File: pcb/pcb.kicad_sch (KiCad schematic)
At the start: 44 parts, among them J1 GPS Module Breakout, J2 MicroSD Card Breakout, U1 XIAO-ESP32-C5-DIP, U10 XIAO-ESP32-C5-DIP, U11 XIAO-ESP32-C5-DIP, U12 XIAO-ESP32-C5-DIP, U13 XIAO-ESP32-C5-DIP, U14 XIAO-ESP32-C5-DIP, U15 XIAO-ESP32-C5-DIP, U16 XIAO-ESP32-C5-DIP, U17 ESP32-S3 DevKitC-1, U18 LD1117V33, U19 SN74HC125N, U2 XIAO-ESP32-C5-DIP, U20 SN74HC138N, U21 SN74HC138N, U3 XIAO-ESP32-C5-DIP, U4 XIAO-ESP32-C5-DIP, U5 XIAO-ESP32-C5-DIP, U6 XIAO-ESP32-C5-DIP, U7 XIAO-ESP32-C5-DIP, U8 XIAO-ESP32-C5-DIP, U9 XIAO-ESP32-C5-DIP

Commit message: implement more feedback from red :D
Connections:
- net +5V: no longer U20.16 (VCC), U20.6 (G1), U21.16 (VCC)
- net CS 00: now also J2.1 (Pin_1); no longer C2.1, J2.6 (Pin_6), R1.1, U19.12 (4A)
- net GND: now also C2.2, U19.12 (4A)
- net +3.3V: now reaches C3.2, U18.2 (VO), U19.14 (VCC)
- net +3.3V: now also C2.1, J2.6 (Pin_6), R1.1, U20.16 (VCC), U20.6 (G1), U21.16 (VCC); no longer C2.2
- net at U19.11 (4Y): no longer J2.1 (Pin_1)
- no-connect marks 143 -> 144
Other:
- moved on the sheet: C2

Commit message: Add brownout protection
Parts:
- added C4: 47uF, Capacitor_THT:C_Disc_D5.0mm_W2.5mm_P2.50mm, symbol Device:C
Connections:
- net +5V: now also C4.2
- net GND: now also C4.1
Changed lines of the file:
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@@
 	)
 	(junction
+		(at 196.85 34.29)
+		(diameter 0)
+		(color 0 0 0 0)
+	)
+	(junction
 		(at 226.06 129.54)
 		(diameter 0)
@@
 	)
 	(junction
+		(at 196.85 24.13)
+		(diameter 0)
+		(color 0 0 0 0)
+	)
+	(junction
 		(at 87.63 212.09)
 		(diameter 0)
@@
 	(wire
 		(pts
+			(xy 204.47 25.4) (xy 196.85 25.4)
+		)
+		(stroke
+			(width 0)
+			(type default)
+		)
+	)
+	(wire
+		(pts
 			(xy 87.63 22.86) (xy 73.66 22.86)
 		)
@@
 	(wire
 		(pts
+			(xy 196.85 33.02) (xy 196.85 34.29)
+		)
+		(stroke
+			(width 0)
+			(type default)
+		)
+	)
+	(wire
+		(pts
 			(xy 226.06 191.77) (xy 226.06 207.01)
 		)
@@
 	(wire
 		(pts
+			(xy 196.85 25.4) (xy 196.85 24.13)
+		)
+		(stroke
+			(width 0)
+			(type default)
+		)
+	)
+	(wire
+		(pts
 			(xy 280.67 240.03) (xy 278.13 240.03)
 		)
@@
 	(wire
 		(pts
+			(xy 204.47 33.02) (xy 196.85 33.02)
+		)
+		(stroke
+			(width 0)
+			(type default)
+		)
+	)
+	(wire
+		(pts
 			(xy 133.35 143.51) (xy 133.35 147.32)
 		)
@@
 					(unit 1)
 				)
+			)
+		)
+	)
+	(symbol
+		(lib_id "Device:C")
+		(at 204.47 29.21 180)
+		(unit 1)
+		(body_style 1)
+		(exclude_from_sim no)
+		(in_bom yes)
+		(on_board yes)
+		(in_pos_files yes)
+		(dnp no)
+		(fields_autoplaced yes)
+		(property "Reference" "C4"
+			(at 208.28 27.9399 0)
+			(show_name no)
+			(do_not_autoplace no)
+			(effects
+				(font
+					(size 1.27 1.27)
+				)
+				(justify right)
+			)
+		)
+		(property "Value" "47uF"
+			(at 208.28 30.4799 0)
+			(show_name no)
+			(do_not_autoplace no)
+			(effects
+				(font
+					(size 1.27 1.27)
+				)
+				(justify right)
+			)
+		)
+		(property "Footprint" "Capacitor_THT:C_Disc_D5.0mm_W2.5mm_P2.50mm"
+			(at 203.5048 25.4 0)
+			(hide yes)
+			(show_name no)
+			(do_not_autoplace no)
+			(effects
+				(font
+					(size 1.27 1.27)
+				)
+			)
+		)
+		(property "Datasheet" ""
+			(at 204.47 29.21 0)
+			(hide yes)
+			(show_name no)
+			(do_not_autoplace no)
+			(effects
+				(font
+					(size 1.27 1.27)
+				)
+			)
+		)
+		(property "Description" "Unpolarized capacitor"
+			(at 204.47 29.21 0)
+			(hide yes)
+			(show_name no)
+			(do_not_autoplace no)
+			(effects
+				(font
+					(size 1.27 1.27)
+				)
+			)
+		)
+		(pin "1"
+		)
+		(pin "2"
+		)
+		(instances
+			(project "pcb"
+				(path "/177b52ef-cce2-4dab-a936-75649664352c"
+					(reference "C4")
+					(unit 1)
+				)

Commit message: Thicker tracks, remove redundant ground lines, mounting holes
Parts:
- added H1, H2, H3, H4: MountingHole, MountingHole:MountingHole_3.2mm_M3, symbol Mechanical:MountingHole

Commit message: Fix 15/16 ordering
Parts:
- renumbered R2 to R1, R11 to R10, R12 to R11, R13 to R12, R14 to R13, R15 to R14, R16 to R15, R17 to R16, R1 to R17, R3 to R2, R4 to R3, R5 to R4, R6 to R5, R7 to R6, R8 to R7, R9 to R8, R10 to R9, U16 to U15, U15 to U16
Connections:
- net CS 15: now also R15.2, U15.3 (GPIO25_D2); no longer R16.2, U16.3 (GPIO25_D2)
- net CS 16: now also R16.2, U16.3 (GPIO25_D2); no longer R15.2, U15.3 (GPIO25_D2)
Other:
- moved on the sheet: R15, R16, U15, U16

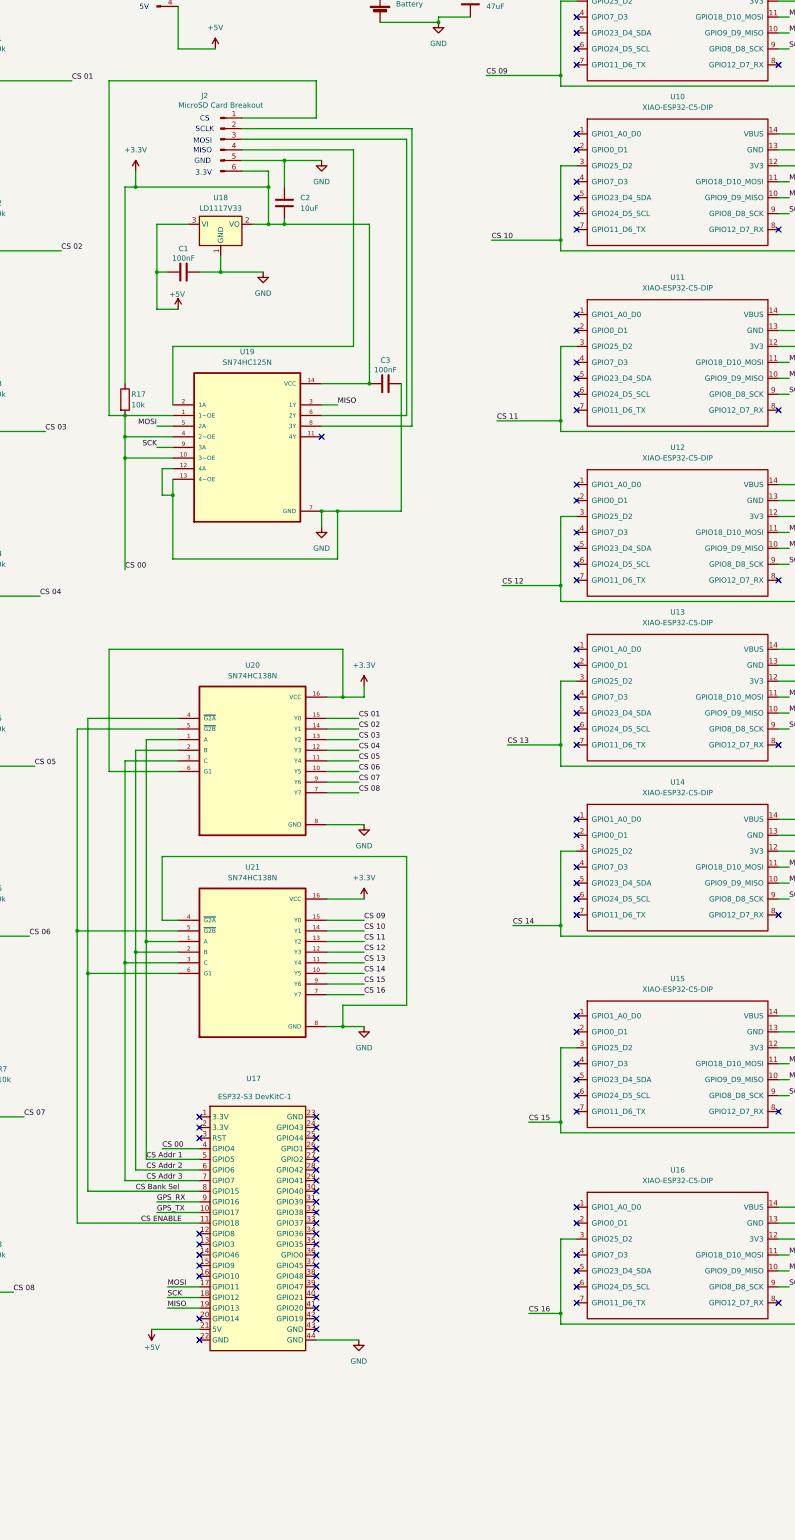
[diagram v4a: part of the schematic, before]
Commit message: add exhaust fan power
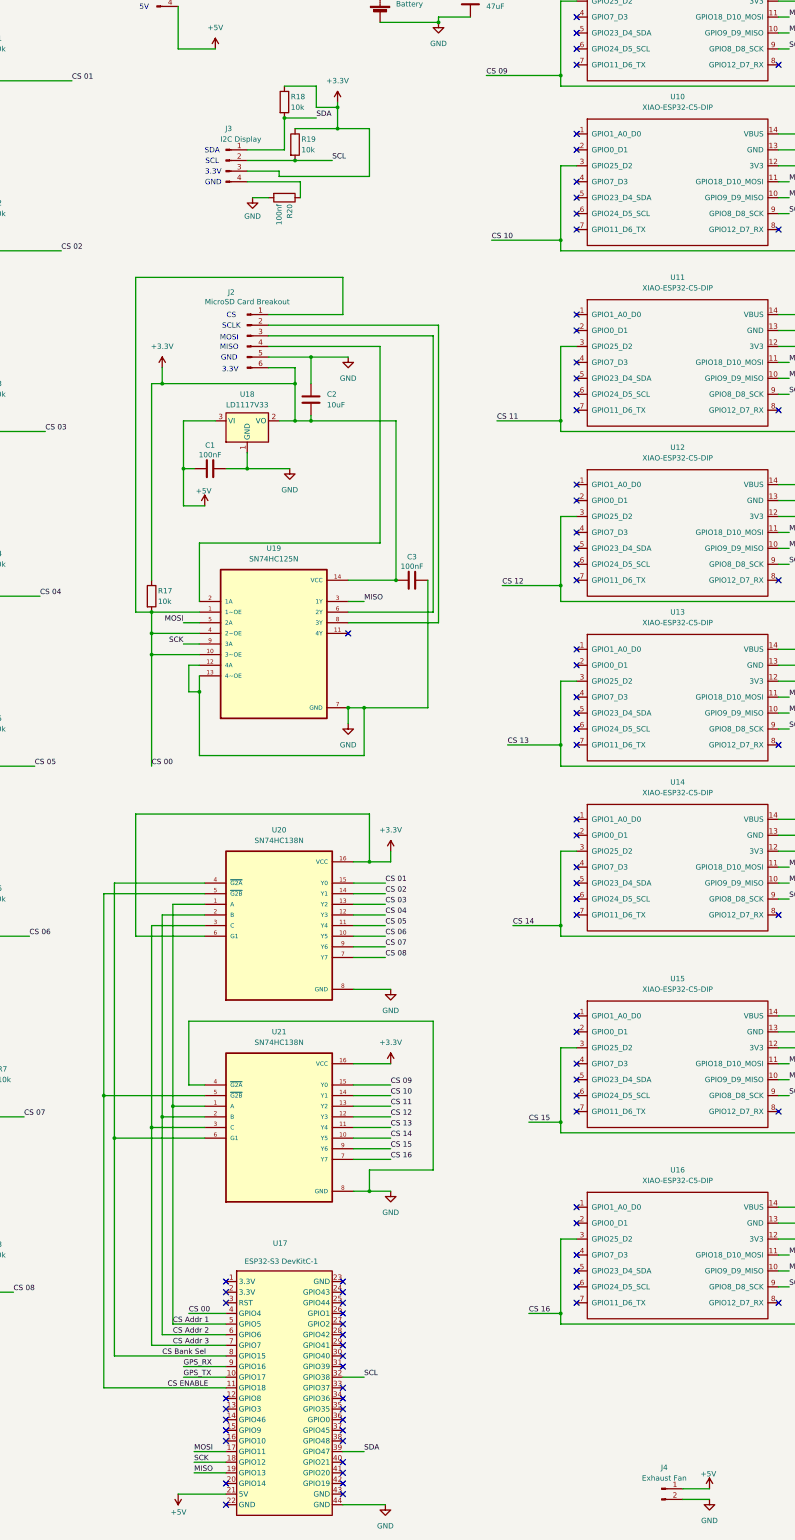
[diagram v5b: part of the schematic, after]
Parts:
- added J3: I2C Display, Connector_PinHeader_2.54mm:PinHeader_1x04_P2.54mm_Vertical, symbol Connector:Conn_01x04_Pin
- added J4: Exhaust Fan, Connector_PinHeader_2.54mm:PinHeader_1x02_P2.54mm_Vertical, symbol Connector:Conn_01x02_Pin
- added R18, R19: 10k, Resistor_THT:R_Axial_DIN0204_L3.6mm_D1.6mm_P5.08mm_Horizontal, symbol Device:R
- added R20: 100nf, Resistor_THT:R_Axial_DIN0204_L3.6mm_D1.6mm_P5.08mm_Horizontal, symbol Device:R
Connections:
- net +3.3V: now also J3.3 (Pin_3), R18.1, R19.1
- net +5V: now also J4.1 (Pin_1)
- net GND: now also J4.2 (Pin_2), R20.2
- net SCL: now reaches U17.32 (GPIO38)
- net SCL: now also J3.2 (Pin_2), R19.2
- net SDA: now reaches U17.39 (GPIO47)
- net SDA: now also J3.1 (Pin_1), R18.2
- new net: J3.4 (Pin_4), R20.1
- no-connect marks 144 -> 142
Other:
- note added: "SCL"
- note added: "SDA"
- moved on the sheet: C1, C2, C3, J2, R17, U17, U18, U19, U20, U21

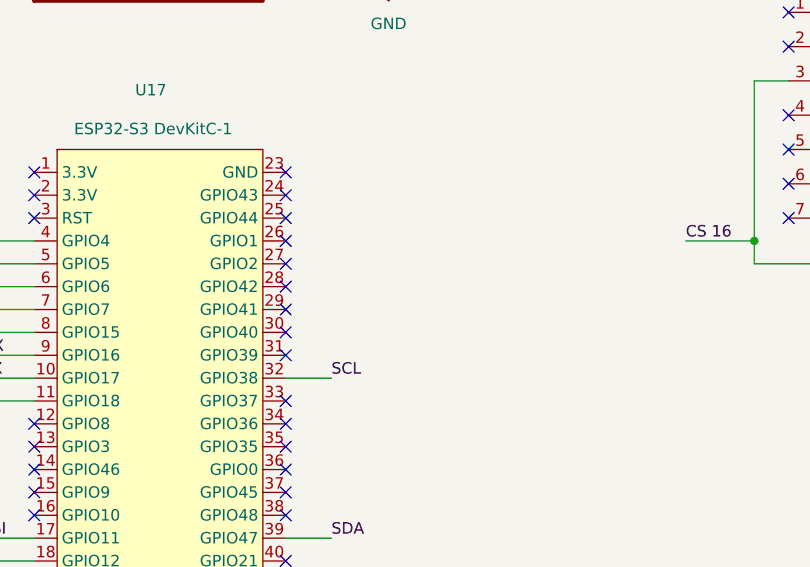
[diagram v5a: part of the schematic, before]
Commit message: Add input buttons for some future use
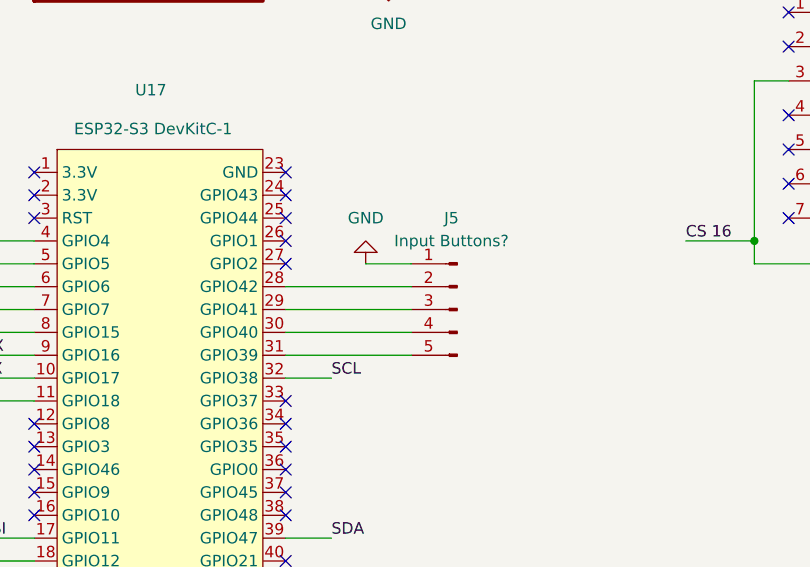
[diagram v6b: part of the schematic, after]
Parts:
- added J5: Input Buttons?, Connector_PinHeader_2.54mm:PinHeader_1x04_P2.54mm_Vertical, symbol Connector:Conn_01x05_Pin
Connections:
- net GND: now also J5.1 (Pin_1)
- net at U17.28 (GPIO42): now also J5.2 (Pin_2)
- net at U17.29 (GPIO41): now also J5.3 (Pin_3)
- net at U17.30 (GPIO40): now also J5.4 (Pin_4)
- net at U17.31 (GPIO39): now also J5.5 (Pin_5)
- no-connect marks 142 -> 138
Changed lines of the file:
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@@
 	)
 	(no_connect
-		(at 173.99 350.52)
-	)
-	(no_connect
 		(at 73.66 128.27)
 	)
@@
 	)
 	(no_connect
-		(at 173.99 353.06)
-	)
-	(no_connect
 		(at 146.05 335.28)
 	)
@@
 	)
 	(no_connect
-		(at 173.99 347.98)
-	)
-	(no_connect
 		(at 173.99 373.38)
 	)
@@
 	)
 	(no_connect
-		(at 173.99 355.6)
-	)
-	(no_connect
 		(at 26.67 284.48)
 	)
@@
 	(wire
 		(pts
+			(xy 173.99 355.6) (xy 187.96 355.6)
+		)
+		(stroke
+			(width 0)
+			(type default)
+		)
+	)
+	(wire
+		(pts
 			(xy 287.02 232.41) (xy 287.02 237.49)
 		)
@@
 	(wire
 		(pts
+			(xy 173.99 353.06) (xy 187.96 353.06)
+		)
+		(stroke
+			(width 0)
+			(type default)
+		)
+	)
+	(wire
+		(pts
+			(xy 182.88 345.44) (xy 187.96 345.44)
+		)
+		(stroke
+			(width 0)
+			(type default)
+		)
+	)
+	(wire
+		(pts
 			(xy 218.44 297.18) (xy 226.06 297.18)
 		)
@@
 	(wire
 		(pts
+			(xy 173.99 347.98) (xy 187.96 347.98)
+		)
+		(stroke
+			(width 0)
+			(type default)
+		)
+	)
+	(wire
+		(pts
 			(xy 21.59 153.67) (xy 21.59 173.99)
 		)
@@
 	(wire
 		(pts
+			(xy 173.99 350.52) (xy 187.96 350.52)
+		)
+		(stroke
+			(width 0)
+			(type default)
+		)
+	)
+	(wire
+		(pts
 			(xy 175.26 167.64) (xy 186.69 167.64)
 		)
@@
 	)
 	(symbol
+		(lib_id "power:GND")
+		(at 182.88 345.44 0)
+		(mirror x)
+		(unit 1)
+		(body_style 1)
+		(exclude_from_sim no)
+		(in_bom yes)
+		(on_board yes)
+		(in_pos_files yes)
+		(dnp no)
+		(fields_autoplaced yes)
+		(property "Reference" "#PWR052"
+			(at 182.88 339.09 0)
+			(hide yes)
+			(show_name no)
+			(do_not_autoplace no)
+			(effects
+				(font
+					(size 1.27 1.27)
+				)
+			)
+		)
+		(property "Value" "GND"
+			(at 182.88 340.36 0)
+			(show_name no)
+			(do_not_autoplace no)
+			(effects
+				(font
+					(size 1.27 1.27)
+				)
+			)
+		)
+		(property "Footprint" ""
+			(at 182.88 345.44 0)
+			(hide yes)
+			(show_name no)
+			(do_not_autoplace no)
+			(effects
+				(font
+					(size 1.27 1.27)
+				)
+			)
+		)
+		(property "Datasheet" ""
+			(at 182.88 345.44 0)
+			(hide yes)
+			(show_name no)
+			(do_not_autoplace no)
+			(effects
+				(font
+					(size 1.27 1.27)
+				)
+			)
+		)
+		(property "Description" "Power symbol creates a global label with name \"GND\" , ground"
+			(at 182.88 345.44 0)
+			(hide yes)
+			(show_name no)
+			(do_not_autoplace no)
+			(effects
+				(font
+					(size 1.27 1.27)
+				)
+			)
+		)
+		(pin "1"
+		)
+		(instances
+			(project "pcb"
+				(path "/177b52ef-cce2-4dab-a936-75649664352c"
+					(reference "#PWR052")
+					(unit 1)
+				)
+			)
+		)
+	)
+	(symbol
 		(lib_id "power:+3.3V")
 		(at 185.42 283.21 0)
@@
 					(unit 1)
 				)
+			)
+		)
+	)
+	(symbol
+		(lib_id "Connector:Conn_01x05_Pin")
+		(at 193.04 350.52 0)
+		(mirror y)
+		(unit 1)
+		(body_style 1)
+		(exclude_from_sim no)
+		(in_bom yes)
+		(on_board yes)
+		(in_pos_files yes)
+		(dnp no)
+		(fields_autoplaced yes)
+		(property "Reference" "J5"
+			(at 192.405 340.36 0)
+			(show_name no)
+			(do_not_autoplace no)
+			(effects
+				(font
+					(size 1.27 1.27)
+				)
+			)
+		)
+		(property "Value" "Input Buttons?"
+			(at 192.405 342.9 0)
+			(show_name no)
+			(do_not_autoplace no)
+			(effects
+				(font
+					(size 1.27 1.27)
+				)
+			)
+		)
+		(property "Footprint" "Connector_PinHeader_2.54mm:PinHeader_1x04_P2.54mm_Vertical"
+			(at 193.04 350.52 0)
+			(hide yes)
+			(show_name no)
+			(do_not_autoplace no)
+			(effects
+				(font
+					(size 1.27 1.27)
+				)
+			)
+		)
+		(property "Datasheet" ""
+			(at 193.04 350.52 0)
+			(hide yes)
+			(show_name no)
+			(do_not_autoplace no)
+			(effects
+				(font
+					(size 1.27 1.27)
+				)
+			)
+		)
+		(property "Description" "Generic connector, single row, 01x05, script generated"
+			(at 193.04 350.52 0)
+			(hide yes)
+			(show_name no)
+			(do_not_autoplace no)
+			(effects
+				(font
+					(size 1.27 1.27)
+				)
+			)
+		)
+		(pin "5"
+		)
+		(pin "3"
+		)
+		(pin "4"
+		)
+		(pin "2"
+		)
+		(pin "1"
+		)
+		(instances
+			(project "pcb"
+				(path "/177b52ef-cce2-4dab-a936-75649664352c"
+					(reference "J5")
+					(unit 1)
+				)
